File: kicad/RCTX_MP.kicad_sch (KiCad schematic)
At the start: 30 parts

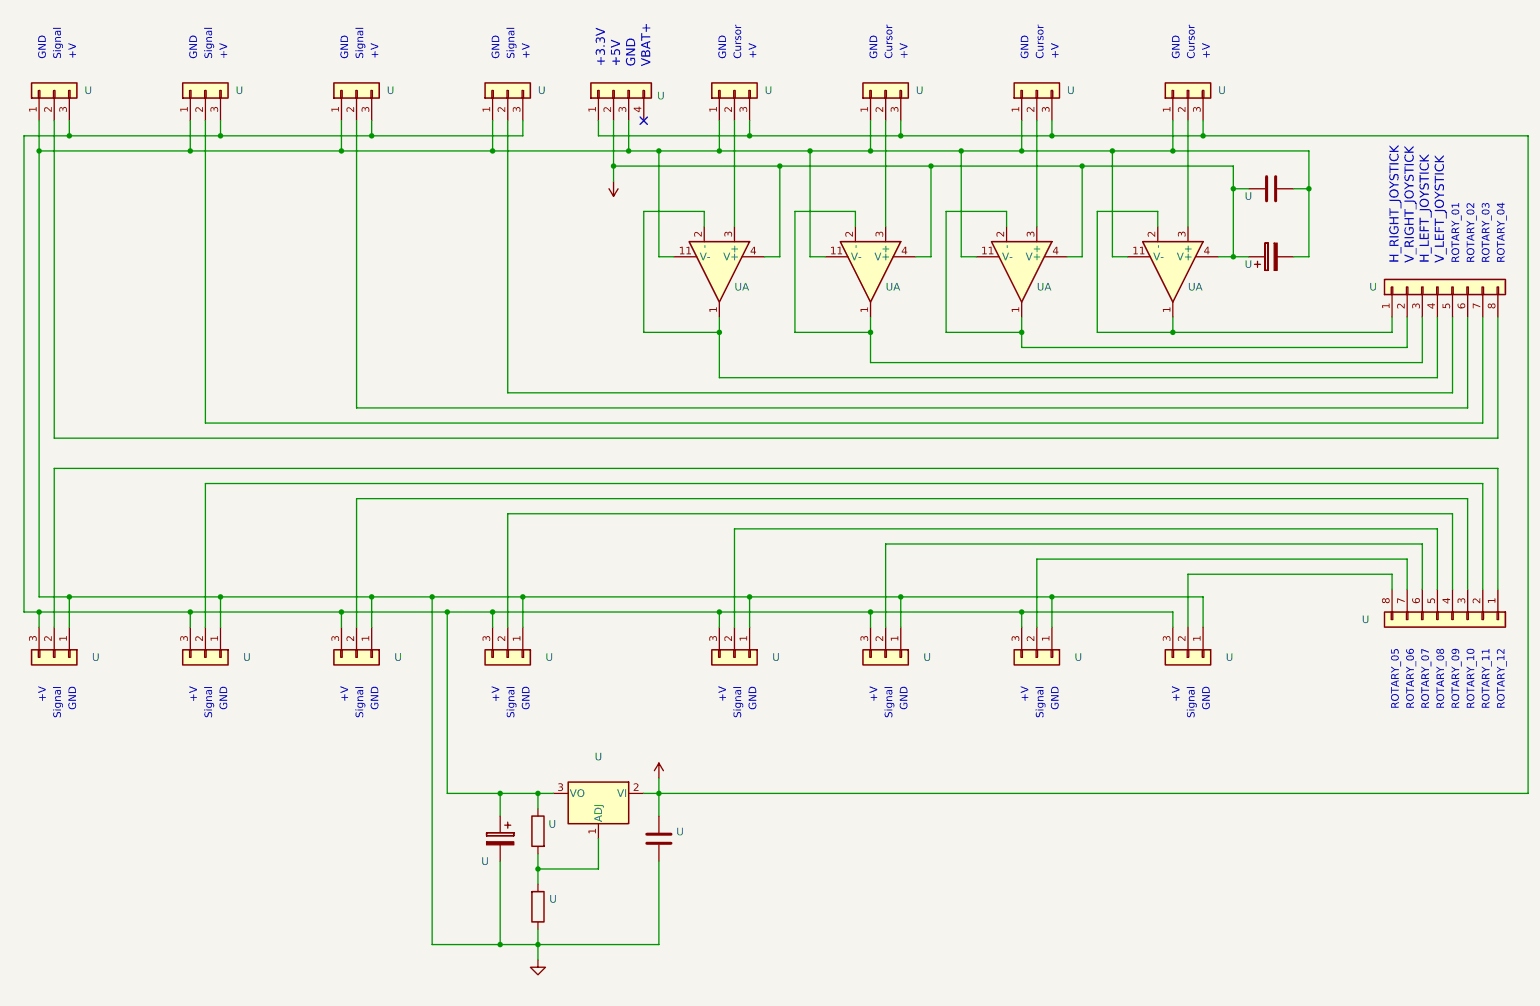
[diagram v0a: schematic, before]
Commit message: Adding PIB USB BRIDGE UML state diagrams - WIP
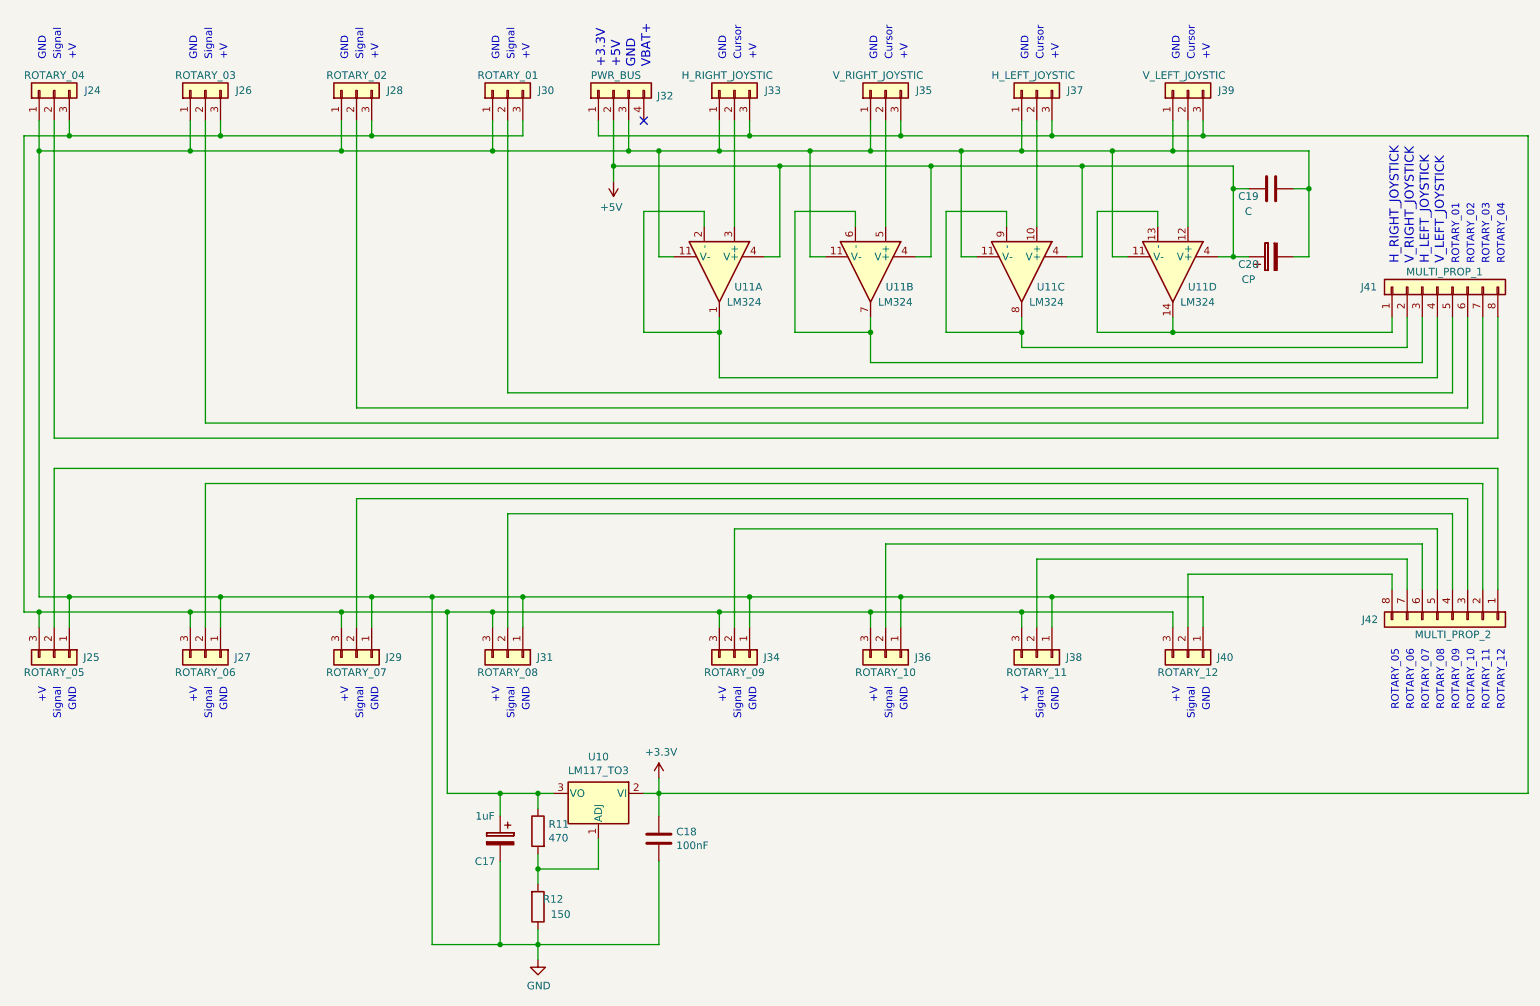
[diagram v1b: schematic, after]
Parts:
- C17: renamed from U; value (none) -> 1uF; footprint (none) -> Capacitors_THT:CP_Radial_D5.0mm_P2.50mm
- C18: renamed from U; value (none) -> 100nF; footprint (none) -> Capacitors_THT:C_Disc_D3.0mm_W1.6mm_P2.50mm
- C19: renamed from U; value (none) -> C; footprint (none) -> Capacitors_THT:C_Disc_D3.0mm_W1.6mm_P2.50mm
- C20: renamed from U; value (none) -> CP; footprint (none) -> Capacitors_THT:CP_Radial_D5.0mm_P2.50mm
- J24: renamed from U; value (none) -> ROTARY_04; footprint (none) -> servo_conn:SRV_1
- J25: renamed from U; value (none) -> ROTARY_05; footprint (none) -> servo_conn:SRV_1
- J26: renamed from U; value (none) -> ROTARY_03; footprint (none) -> servo_conn:SRV_1
- J27: renamed from U; value (none) -> ROTARY_06; footprint (none) -> servo_conn:SRV_1
- J28: renamed from U; value (none) -> ROTARY_02; footprint (none) -> servo_conn:SRV_1
- J29: renamed from U; value (none) -> ROTARY_07; footprint (none) -> servo_conn:SRV_1
- J30: renamed from U; value (none) -> ROTARY_01; footprint (none) -> servo_conn:SRV_1
- J31: renamed from U; value (none) -> ROTARY_08; footprint (none) -> servo_conn:SRV_1
- J32: renamed from U; value (none) -> PWR_BUS; footprint (none) -> Connectors_Samtec:SL-104-X-XX_1x04
- J33: renamed from U; value (none) -> H_RIGHT_JOYSTIC; footprint (none) -> servo_conn:SRV_1
- J34: renamed from U; value (none) -> ROTARY_09; footprint (none) -> servo_conn:SRV_1
- J35: renamed from U; value (none) -> V_RIGHT_JOYSTIC; footprint (none) -> servo_conn:SRV_1
- J36: renamed from U; value (none) -> ROTARY_10; footprint (none) -> servo_conn:SRV_1
- J37: renamed from U; value (none) -> H_LEFT_JOYSTIC; footprint (none) -> servo_conn:SRV_1
- J38: renamed from U; value (none) -> ROTARY_11; footprint (none) -> servo_conn:SRV_1
- J39: renamed from U; value (none) -> V_LEFT_JOYSTIC; footprint (none) -> servo_conn:SRV_1
- J40: renamed from U; value (none) -> ROTARY_12; footprint (none) -> servo_conn:SRV_1
- J41: renamed from U; value (none) -> MULTI_PROP_1; footprint (none) -> Connectors_Samtec:SL-108-X-XX_1x08
- J42: renamed from U; value (none) -> MULTI_PROP_2; footprint (none) -> Connectors_Samtec:SL-108-X-XX_1x08
- R11: renamed from U; value (none) -> 470; footprint (none) -> Resistors_THT:R_Axial_DIN0204_L3.6mm_D1.6mm_P1.90mm_Vertical
- R12: renamed from U; value (none) -> 150; footprint (none) -> Resistors_THT:R_Axial_DIN0204_L3.6mm_D1.6mm_P1.90mm_Vertical
- U10: renamed from U; value (none) -> LM117_TO3; footprint (none) -> TO_SOT_Packages_THT:TO-92_Inline_Narrow_Oval
- U11: renamed from U; value (none) -> LM324; footprint (none) -> Housings_DIP:DIP-14_W7.62mm
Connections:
- net at J35.2 (Pin_2): now also U11.5 (+); no longer U11.3 (+)
- net at J37.2 (Pin_2): now also U11.10 (+); no longer U11.3 (+)
- net at J39.2 (Pin_2): now also U11.12 (+); no longer U11.3 (+)
- new net: J41.3 (Pin_3), U11.6 (-), U11.7
- new net: J41.2 (Pin_2), U11.8, U11.9 (-)
- new net: J41.1 (Pin_1), U11.13 (-), U11.14
